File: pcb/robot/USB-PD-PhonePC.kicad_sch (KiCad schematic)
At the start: 1 part, among them J9 Conn_01x16

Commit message: JLCPCB Update and Verification
The Gerber files were updated, DNP and exclude were removed, Gerber files were uploaded and configured to JLCPCB, Pick and Place and BOM were added, devices were replaced, and factory stock was verified. The price and estimated manufacturing time were obtained.
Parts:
- J9: now left out of the parts list
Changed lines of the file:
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@@
 		(unit 1)
 		(exclude_from_sim no)
-		(in_bom yes)
+		(in_bom no)
 		(on_board yes)
 		(dnp no)

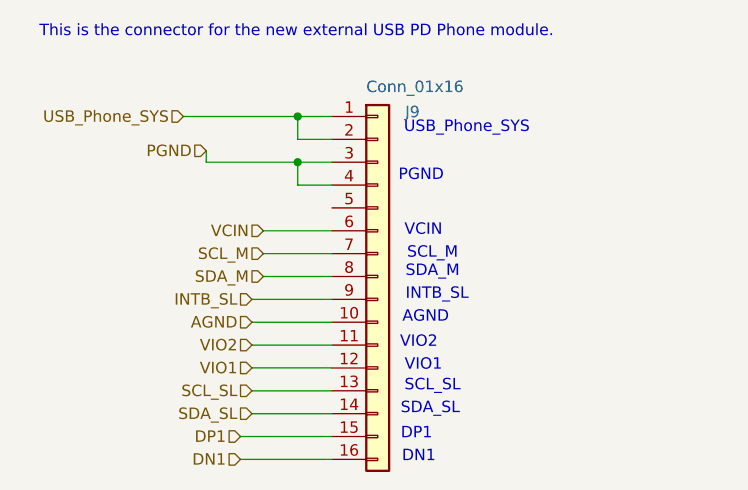
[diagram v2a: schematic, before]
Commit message: Modification and replacement of MAX77642ANA
The MAX77642ANA was replaced with the LDO XC6206 and the TPS63021DSJR. Rerouting and Gerber updates were performed.
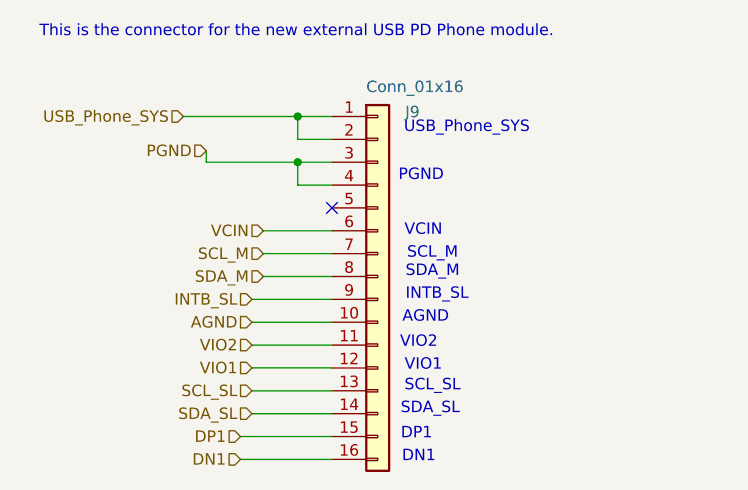
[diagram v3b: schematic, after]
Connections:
- no-connect marks 0 -> 1
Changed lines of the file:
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@@
 		(color 0 0 0 0)
+	)
+	(no_connect
+		(at 293.37 195.58)
 	)
 	(wire
